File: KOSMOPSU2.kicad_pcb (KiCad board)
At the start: 2 copper layers, 153.7 x 73.9 mm, 24 parts, among them J1 Conn_01x03_Male, J2 Conn_02x05_Odd_Even, J3 Conn_01x03_Male, T1 Transformer_1P_2S, U1 L7812, U2 L7912

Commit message: autosync
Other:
- board text added: "Claytune Power Supply By Twinturbo V1.0"
- board text removed: "Claytune Power Supply By Twinturbo V.01"
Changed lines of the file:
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@@
-(kicad_pcb (version 20171130) (host pcbnew "(5.1.5)-3")
+(kicad_pcb (version 20171130) (host pcbnew 5.1.5-52549c5~86~ubuntu18.04.1)
   (general
     (thickness 1.6)
@@
     (effects (font (size 1.5 2) (thickness 0.3)))
   )
-  (gr_text "Claytune Power Supply \nBy Twinturbo\nV.01" (at 159.42 56.23) (layer F.SilkS)
+  (gr_text "Claytune Power Supply \nBy Twinturbo\nV1.0" (at 159.42 56.23) (layer F.SilkS)
     (effects (font (size 2 2) (thickness 0.3)))
   )

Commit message: autosync
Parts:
- T1: value Transformer_1P_2S -> Myrra 44440 Transformer 240V
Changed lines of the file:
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@@
       (effects (font (size 1 1) (thickness 0.15)))
     )
-    (fp_text value Transformer_1P_2S (at 33.02 36.068 90) (layer F.SilkS)
+    (fp_text value "Myrra 44440 Transformer 240V " (at 31.864 26.27 90) (layer F.SilkS)
       (effects (font (size 1 1) (thickness 0.15)))
     )

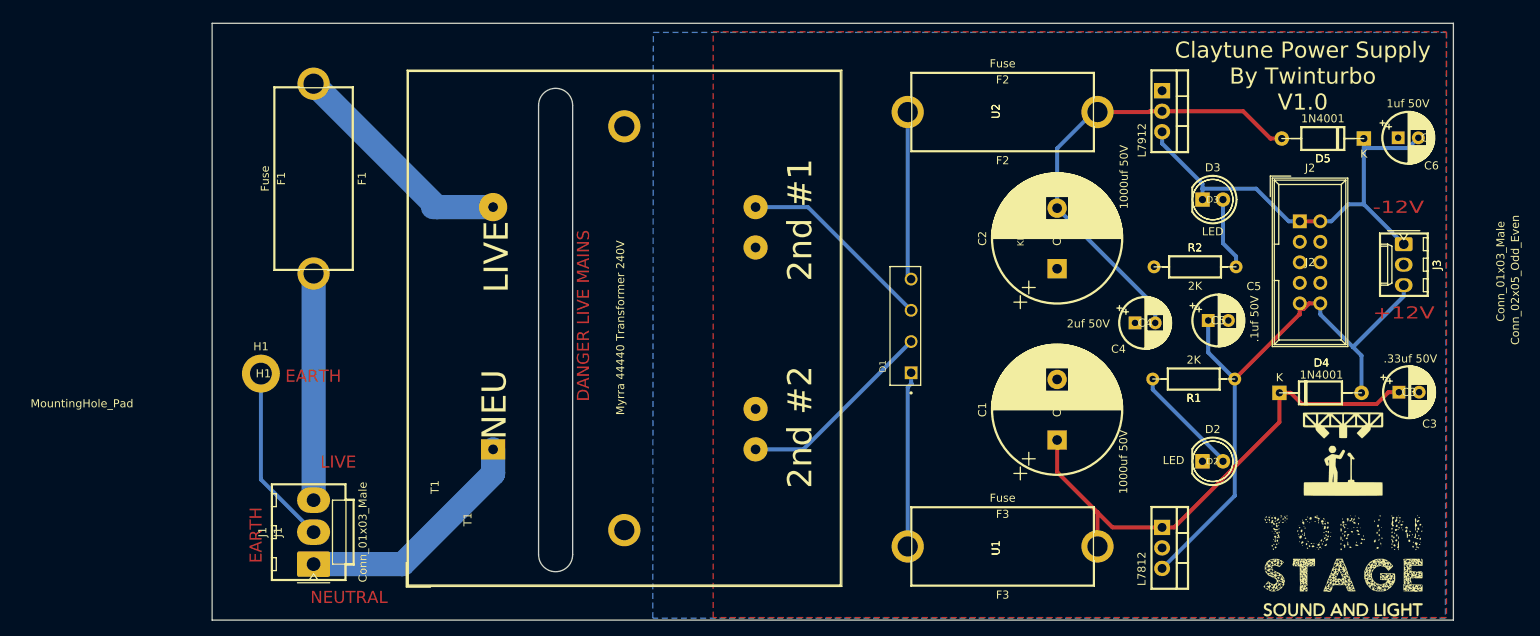
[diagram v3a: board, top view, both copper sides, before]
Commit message: Mounting Holes On PCB
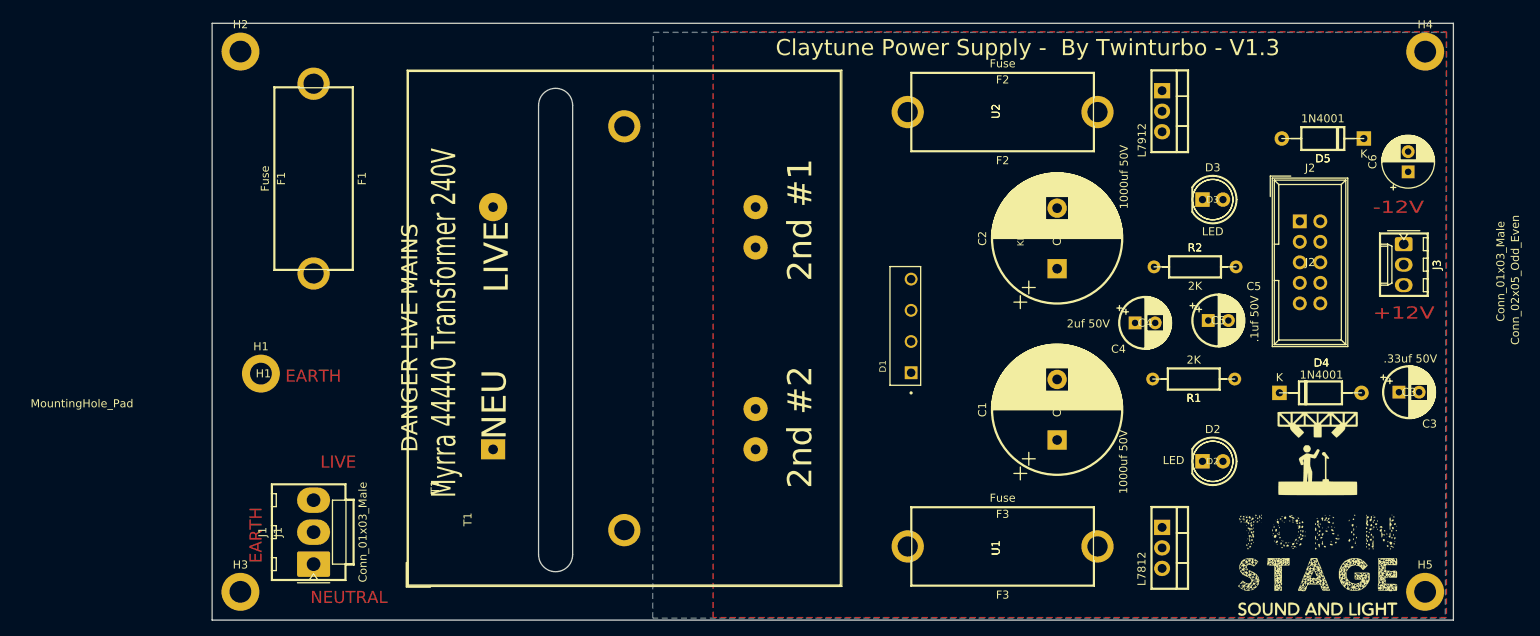
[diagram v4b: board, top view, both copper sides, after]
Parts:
- removed the G*** at (164.5, 110.6)
- added G***: LOGO, AA-ROB:GX-TOBINLOGO, F.Cu at (161.3, 110.5)
- added H2: MountingHole_Pad, MountingHole:MountingHole_2.7mm_M2.5_DIN965_Pad, F.Cu at (27.9, 53.2)
- added H3: MountingHole_Pad, MountingHole:MountingHole_2.7mm_M2.5_DIN965_Pad, F.Cu at (27.9, 120.1)
- added H4: MountingHole_Pad, MountingHole:MountingHole_2.7mm_M2.5_DIN965_Pad, F.Cu at (174.6, 53.2)
- added H5: MountingHole_Pad, MountingHole:MountingHole_2.7mm_M2.5_DIN965_Pad, F.Cu at (174.6, 120.1)
- F2, F3: footprint ROBSLIBRARY:googiefuse -> AA-ROB:PCB-20MM-FUSE-HOLDER
- moved C6 4.39 mm to (172.5, 68.1), turned to 90 degrees
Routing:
- net +12V: track 74.8 -> 0.00 mm
- net Net-(C1-Pad1): track 63.6 -> 0.00 mm
- net Net-(C2-Pad2): track 58.3 -> 0.00 mm
- net -12V: track 55.4 -> 0.00 mm
- net NEUT: track 29.9 -> 0.00 mm
- net Net-(F1-Pad1): track 29.1 -> 0.00 mm
- net LINE: track 28.1 -> 0.00 mm
- net Net-(D1-Pad2): track 24.8 -> 0.00 mm
- net Net-(D1-Pad3): track 24.6 -> 0.00 mm
- net Earth: track 22.3 -> 0.00 mm
- net Net-(D1-Pad1): track 21.8 -> 0.00 mm
- net Net-(D1-Pad4): track 20.9 -> 0.00 mm
- net Net-(D2-Pad2): track 13.8 -> 0.00 mm
- net Net-(D3-Pad2): track 9.00 -> 0.00 mm
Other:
- board text added: "Claytune Power Supply - By Twinturbo - V1.3"
- board text removed: "Claytune Power Supply By Twinturbo V1.0"
